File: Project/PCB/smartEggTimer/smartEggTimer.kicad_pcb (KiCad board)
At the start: 2 copper layers, 70 x 70 mm, 0 parts

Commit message: corrections and refinements for the schematic
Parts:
- added C1: 10u, Capacitor_SMD:C_0603_1608Metric, F.Cu at (192.1, 114.6)
- added C10: 4u7, Capacitor_SMD:C_0603_1608Metric, F.Cu at (192.1, 122.1)
- added C11: 4u7, Capacitor_SMD:C_0603_1608Metric, F.Cu at (192.1, 124.6)
- added C12: 10n, Capacitor_SMD:C_0805_2012Metric, F.Cu at (199.5, 141.0)
- added C13: 10n, Capacitor_SMD:C_0805_2012Metric, F.Cu at (199.5, 144.1)
- added C14: 100n, Capacitor_SMD:C_0402_1005Metric, F.Cu at (222.6, 124.8)
- added C15: 1u, Capacitor_SMD:C_0603_1608Metric, F.Cu at (192.1, 127.1)
- added C16: 1u, Capacitor_SMD:C_0603_1608Metric, F.Cu at (192.1, 129.6)
- added C17: 1u, Capacitor_SMD:C_0603_1608Metric, F.Cu at (198.6, 113.5)
- added C18: 1u, Capacitor_SMD:C_0603_1608Metric, F.Cu at (198.6, 116.0)
- added C2: 100n, Capacitor_SMD:C_0402_1005Metric, F.Cu at (222.6, 114.9)
- added C3: 100n, Capacitor_SMD:C_0402_1005Metric, F.Cu at (222.6, 116.9)
- added C4: 100n, Capacitor_SMD:C_0402_1005Metric, F.Cu at (222.6, 118.9)
- added C5: 100n, Capacitor_SMD:C_0402_1005Metric, F.Cu at (222.6, 120.8)
- added C6: 100n, Capacitor_SMD:C_0402_1005Metric, F.Cu at (222.6, 122.8)
- added C7: 10n, Capacitor_SMD:C_0805_2012Metric, F.Cu at (199.5, 138.0)
- added C8: 1u, Capacitor_SMD:C_0603_1608Metric, F.Cu at (192.1, 117.1)
- added C9: 1u, Capacitor_SMD:C_0603_1608Metric, F.Cu at (192.1, 119.6)
- added DFPlayerMini1: ~, custom-parts:DFplayer-Mini, F.Cu at (145.8, 70.5)
- added FB1: 120R, Inductor_SMD:L_0603_1608Metric, F.Cu at (155.7, 83.6)
- added H1: MountingHole, MountingHole:MountingHole_4.3mm_M4, F.Cu at (124.2, 72.3)
- added H2: MountingHole, MountingHole:MountingHole_4.3mm_M4, F.Cu at (120.5, 108.1)
- added H3: MountingHole, MountingHole:MountingHole_4.3mm_M4_DIN965, F.Cu at (172.0, 75.2)
- added H8: MountingHole, MountingHole:MountingHole_4.3mm_M4_DIN965, F.Cu at (172.9, 106.5)
- added J1: Conn_01x05_Pin, Connector_PinHeader_2.54mm:PinHeader_1x05_P2.54mm_Vertical, F.Cu at (132.0, 109.2)
- added J2: Conn_01x02_Pin, Connector_PinHeader_2.54mm:PinHeader_1x01_P2.54mm_Vertical, F.Cu at (168.3, 46.0)
- added J3: Conn_01x02_Pin, Connector_PinHeader_2.54mm:PinHeader_1x01_P2.54mm_Vertical, F.Cu at (168.3, 50.7)
- added J5: Conn_01x02_Socket, Connector_PinHeader_2.54mm:PinHeader_1x02_P2.54mm_Vertical, F.Cu at (115.8, 100.3)
- added J6: Conn_01x02_Socket, Connector_PinHeader_2.54mm:PinHeader_1x02_P2.54mm_Vertical, F.Cu at (117.0, 79.6)
- added J7: Conn_01x03_Pin, Connector_PinHeader_2.54mm:PinHeader_1x03_P2.54mm_Vertical, F.Cu at (150.1, 109.0)
- added OLED-15W-C1: ~, Connector_PinSocket_2.54mm:PinSocket_1x07_P2.54mm_Vertical, F.Cu at (130.8, 63.4)
- added Q1: STP60NF06L, Package_TO_SOT_THT:TO-220-3_Vertical, F.Cu at (127.5, 88.7)
- added R1: 4k7, Resistor_SMD:R_0402_1005Metric, F.Cu at (202.0, 115.6)
- added R10: 10k, Resistor_SMD:R_0402_1005Metric, F.Cu at (209.5, 124.9)
- added R11: 10k, Resistor_SMD:R_0402_1005Metric, F.Cu at (209.5, 126.9)
- added R12: 1M, Resistor_SMD:R_0402_1005Metric, F.Cu at (209.5, 128.9)
- added R13: 1M, Resistor_SMD:R_0402_1005Metric, F.Cu at (209.5, 130.9)
- added R14: 10k, Resistor_SMD:R_0402_1005Metric, F.Cu at (209.5, 132.9)
- added R15: 22k, Resistor_SMD:R_0402_1005Metric, F.Cu at (216.4, 114.9)
- added R16: 10k, Resistor_SMD:R_0402_1005Metric, F.Cu at (216.4, 116.9)
- added R17: 22k, Resistor_SMD:R_0402_1005Metric, F.Cu at (216.4, 118.8)
- added R18: 10k, Resistor_SMD:R_0402_1005Metric, F.Cu at (216.4, 120.8)
- added R19: 22k, Resistor_SMD:R_0402_1005Metric, F.Cu at (216.4, 122.8)
- added R2: 10k, Resistor_SMD:R_0402_1005Metric, F.Cu at (202.0, 117.5)
- added R20: 10k, Resistor_SMD:R_0402_1005Metric, F.Cu at (216.4, 124.8)
- added R21: 22k, Resistor_SMD:R_0402_1005Metric, F.Cu at (216.4, 126.8)
- added R3: 1k, Resistor_SMD:R_0402_1005Metric, F.Cu at (202.0, 119.5)
- added R4: 100k, Resistor_SMD:R_0402_1005Metric, F.Cu at (202.0, 121.5)
- added R5: 100, Resistor_SMD:R_0402_1005Metric, F.Cu at (202.0, 123.5)
- added R6: 4k7, Resistor_SMD:R_0402_1005Metric, F.Cu at (202.0, 125.5)
- added R7: 4k7, Resistor_SMD:R_0402_1005Metric, F.Cu at (202.0, 127.5)
- added R8: 10k, Resistor_SMD:R_0402_1005Metric, F.Cu at (209.6, 115.3)
- added R9: 10k, Resistor_SMD:R_0402_1005Metric, F.Cu at (209.6, 120.7)
- added SW1: SW_Push_Dual, Button_Switch_THT:SW_PUSH_6mm_H9.5mm, F.Cu at (159.6, 64.8)
- added SW2: EC12E24204A2, Rotary_Encoder:RotaryEncoder_Alps_EC12E_Vertical_H20mm, F.Cu at (167.8, 90.9)
- added SW3: SW_Push_Dual, Button_Switch_THT:SW_PUSH_6mm_H13mm, F.Cu at (113.2, 88.8)
- added SW4: SW_Push_Dual, Button_Switch_THT:SW_PUSH_6mm_H13mm, F.Cu at (130.1, 115.2)
- added SW5: SW_Push_Dual, Button_Switch_THT:SW_PUSH_6mm_H13mm, F.Cu at (144.2, 115.2)
- added SW6: SW_Push_Dual, Button_Switch_THT:SW_PUSH_6mm_H13mm, F.Cu at (157.1, 115.4)
- added SW7: SW_SPDT, Button_Switch_THT:SW_Slide_SPDT_Angled_CK_OS102011MA1Q, F.Cu at (146.2, 127.0)
- added U1: STM32F103RET6, Package_QFP:LQFP-64_10x10mm_P0.5mm, F.Cu at (148.1, 91.2)
- added U3: AP7361C-33E, Package_TO_SOT_SMD:SOT-223-3_TabPin2, F.Cu at (151.5, 69.1)
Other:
- board size 70 x 70 mm -> 72 x 72 mm
- board text added: "diameter of the PCB has to be 72mm with 4 holes, each 21.5mm in both direction from the center away The center of the rotary encoder has to be 30mm from the center away the 4 buttons also have a fixed position as soon as we finished the CAD model"
- board text removed: "diameter of the PCB has to be 70mm with 4 holes, each 21.5mm in both direction from the center away The center of the rotary encoder has to be 30mm from the center away the 4 buttons also have a fixed position as soon as we finished the CAD model"

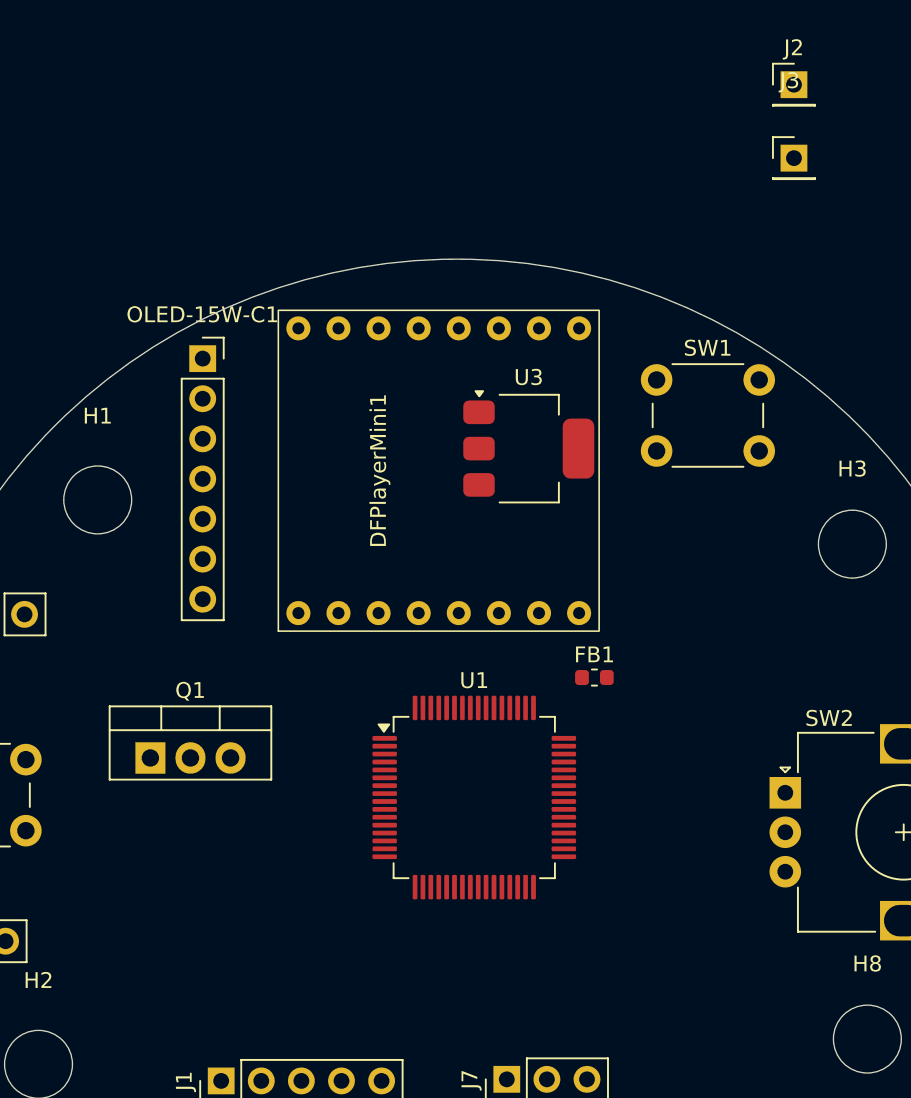
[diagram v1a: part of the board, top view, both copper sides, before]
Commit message: add pin numbers for display
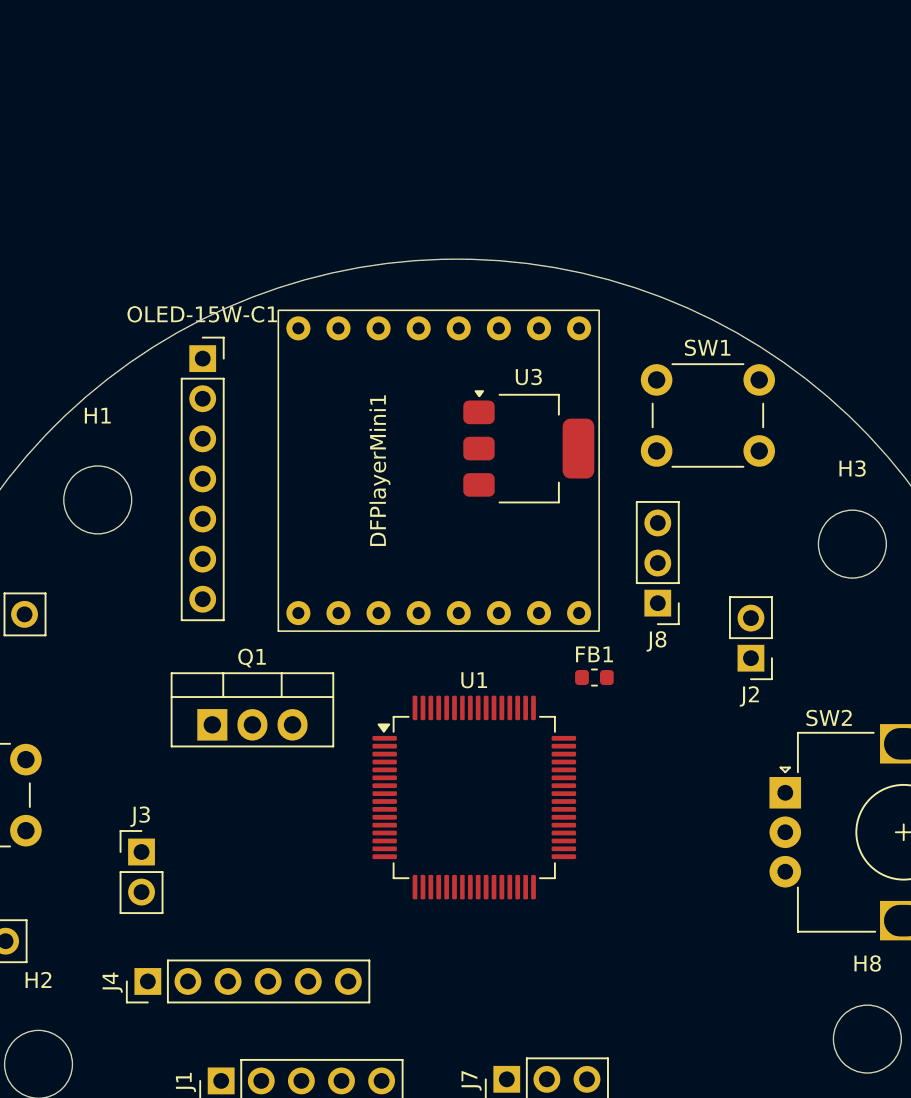
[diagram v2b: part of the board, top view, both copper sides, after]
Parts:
- added J4: Conn_01x06_Pin, Connector_PinHeader_2.54mm:PinHeader_1x06_P2.54mm_Vertical, F.Cu at (127.4, 102.8)
- added J8: Conn_01x03_Pin, Connector_PinHeader_2.54mm:PinHeader_1x03_P2.54mm_Vertical, F.Cu at (159.7, 78.9)
- J2, J3: footprint Connector_PinHeader_2.54mm:PinHeader_1x01_P2.54mm_Vertical -> Connector_PinHeader_2.54mm:PinHeader_1x02_P2.54mm_Vertical
- moved J3 60.3 mm to (127.0, 94.7)
- moved J2 36.4 mm to (165.6, 82.4), turned to 180 degrees
- moved Q1 4.45 mm to (131.5, 86.6)
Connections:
- OLED-15W-C1 pad 1: (no net) -> +3.3V
- OLED-15W-C1 pad 2: (no net) -> GND
- OLED-15W-C1 pad 3: (no net) -> /I2C1_SDA
- OLED-15W-C1 pad 4: (no net) -> /I2C_SCL
- OLED-15W-C1 pad 5: (no net) -> unconnected-(OLED-15W-C1-CS-Pad5)
- OLED-15W-C1 pad 6: (no net) -> unconnected-(OLED-15W-C1-D/C-Pad6)
- OLED-15W-C1 pad 7: (no net) -> /display_reset

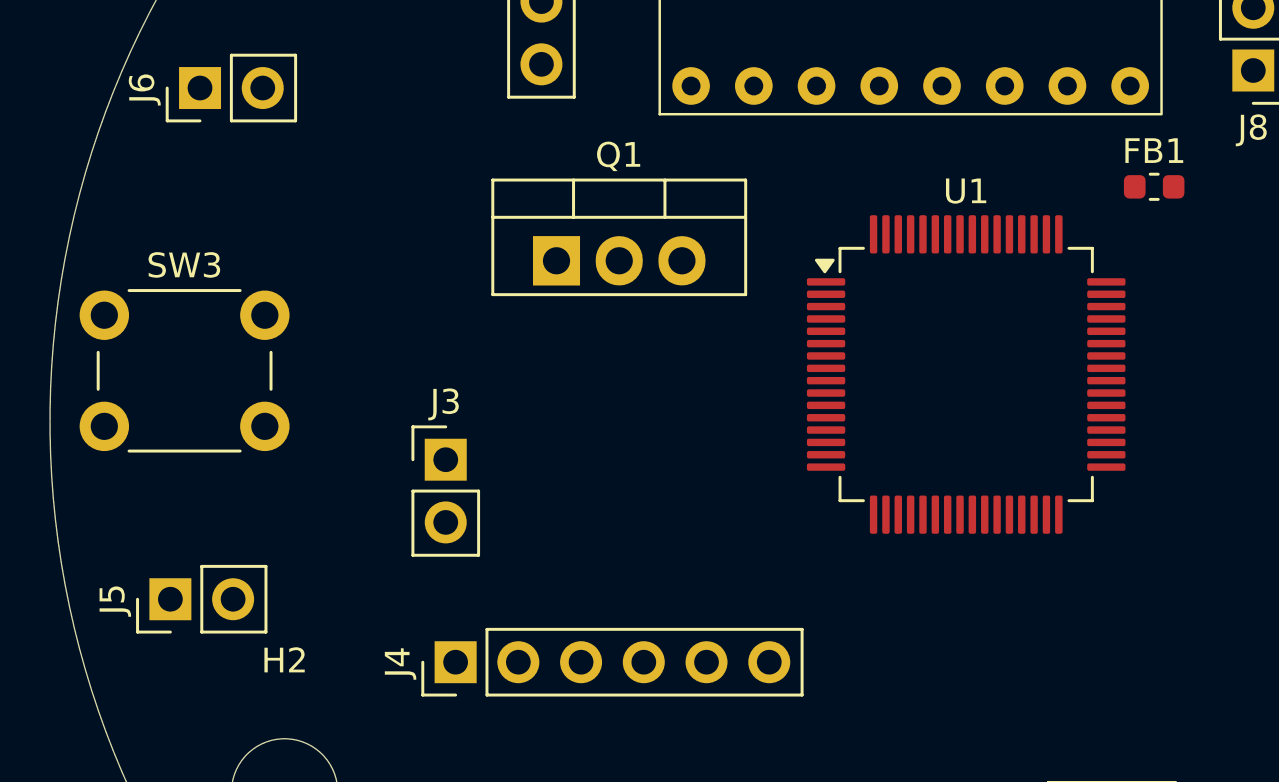
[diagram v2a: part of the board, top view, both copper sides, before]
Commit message: add pin numbers for DFplayer and re-add DFplayer footprint
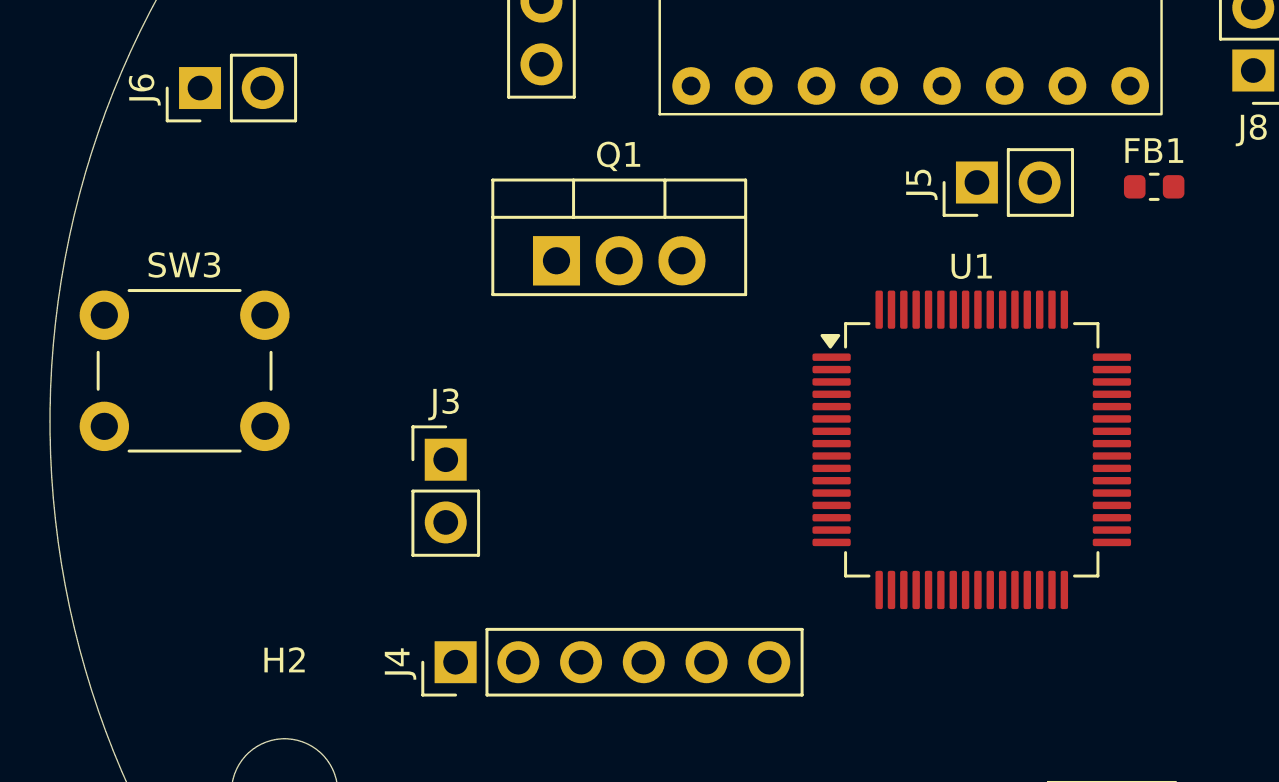
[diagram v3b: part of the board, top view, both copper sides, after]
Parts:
- moved J5 36.8 mm to (148.5, 83.4)
- moved U1 3.06 mm to (148.3, 94.2)
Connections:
- DFPlayerMini1 pad 1: (no net) -> /Battery-SW
- DFPlayerMini1 pad 10: (no net) -> Net-(Q1-D)
- DFPlayerMini1 pad 11: (no net) -> unconnected-(DFPlayerMini1-IO_2-Pad11)
- DFPlayerMini1 pad 12: (no net) -> unconnected-(DFPlayerMini1-ADKEY_1-Pad12)
- DFPlayerMini1 pad 13: (no net) -> unconnected-(DFPlayerMini1-ADKEY_2-Pad13)
- DFPlayerMini1 pad 14: (no net) -> unconnected-(DFPlayerMini1-USB+-Pad14)
- DFPlayerMini1 pad 15: (no net) -> unconnected-(DFPlayerMini1-USB--Pad15)
- DFPlayerMini1 pad 16: (no net) -> unconnected-(DFPlayerMini1-BUSY-Pad16)
- DFPlayerMini1 pad 2: (no net) -> Net-(DFPlayerMini1-RX)
- DFPlayerMini1 pad 3: (no net) -> /UART2_TX
- DFPlayerMini1 pad 4: (no net) -> /DAC_R
- DFPlayerMini1 pad 5: (no net) -> /DAC_L
- DFPlayerMini1 pad 6: (no net) -> /SPK+
- DFPlayerMini1 pad 7: (no net) -> Net-(Q1-D)
- DFPlayerMini1 pad 8: (no net) -> /SPK-
- DFPlayerMini1 pad 9: (no net) -> unconnected-(DFPlayerMini1-IO_1-Pad9)
- Q1 pad 1: Net-(DFPlayerMini1-GND) -> Net-(Q1-D)
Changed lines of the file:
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@@
 	(net 7 "Net-(Q1-G)")
 	(net 8 "/Rotary Encoder b")
-	(net 9 "Net-(DFPlayerMini1-GND)")
+	(net 9 "Net-(Q1-D)")
 	(net 10 "/Battery_indicator")
 	(net 11 "/Button_1")
@@
 	(net 80 "unconnected-(OLED-15W-C1-D{slash}C-Pad6)")
 	(net 81 "unconnected-(OLED-15W-C1-CS-Pad5)")
+	(net 82 "unconnected-(DFPlayerMini1-ADKEY_1-Pad12)")
+	(net 83 "unconnected-(DFPlayerMini1-USB--Pad15)")
+	(net 84 "unconnected-(DFPlayerMini1-IO_2-Pad11)")
+	(net 85 "unconnected-(DFPlayerMini1-IO_1-Pad9)")
+	(net 86 "unconnected-(DFPlayerMini1-BUSY-Pad16)")
+	(net 87 "unconnected-(DFPlayerMini1-USB+-Pad14)")
+	(net 88 "unconnected-(DFPlayerMini1-ADKEY_2-Pad13)")
 	(footprint "Button_Switch_THT:SW_PUSH_6mm_H13mm"
 		(layer "F.Cu")
@@
 			(layers "*.Cu" "*.Mask")
 			(remove_unused_layers no)
+			(net 4 "/Battery-SW")
+			(pinfunction "VCC")
+			(pintype "input")
 		)
 		(pad "2" thru_hole circle
@@
 			(layers "*.Cu" "*.Mask")
 			(remove_unused_layers no)
+			(net 27 "Net-(DFPlayerMini1-RX)")
+			(pinfunction "RX")
+			(pintype "input")
 		)
 		(pad "3" thru_hole circle
@@
 			(layers "*.Cu" "*.Mask")
 			(remove_unused_layers no)
+			(net 59 "/UART2_TX")
+			(pinfunction "TX")
+			(pintype "input")
 		)
 		(pad "4" thru_hole circle
@@
 			(layers "*.Cu" "*.Mask")
 			(remove_unused_layers no)
+			(net 79 "/DAC_R")
+			(pinfunction "DAC_R")
+			(pintype "input")
 		)
 		(pad "5" thru_hole circle
@@
 			(layers "*.Cu" "*.Mask")
 			(remove_unused_layers no)
+			(net 78 "/DAC_L")
+			(pinfunction "DAC_L")
+			(pintype "input")
 		)
 		(pad "6" thru_hole circle
@@
 			(layers "*.Cu" "*.Mask")
 			(remove_unused_layers no)
+			(net 20 "/SPK+")
+			(pinfunction "SPK_1")
+			(pintype "input")
 		)
 		(pad "7" thru_hole circle
@@
 			(layers "*.Cu" "*.Mask")
 			(remove_unused_layers no)
+			(net 9 "Net-(Q1-D)")
+			(pinfunction "GND")
+			(pintype "input")
 		)
 		(pad "8" thru_hole circle
@@
 			(layers "*.Cu" "*.Mask")
 			(remove_unused_layers no)
+			(net 21 "/SPK-")
+			(pinfunction "SPK_2")
+			(pintype "input")
 		)
 		(pad "9" thru_hole circle
-			(at 9.017 -8.89 90)
+			(at 9.017 8.89 90)
 			(size 1.524 1.524)
 			(drill 0.762)
 			(layers "*.Cu" "*.Mask")
 			(remove_unused_layers no)
+			(net 85 "unconnected-(DFPlayerMini1-IO_1-Pad9)")
+			(pinfunction "IO_1")
+			(pintype "input+no_connect")
 		)
 		(pad "10" thru_hole circle
-			(at 9.017 -6.35 90)
+			(at 9.017 6.35 90)
 			(size 1.524 1.524)
 			(drill 0.762)
 			(layers "*.Cu" "*.Mask")
 			(remove_unused_layers no)
+			(net 9 "Net-(Q1-D)")
+			(pinfunction "GND")
+			(pintype "input")
 		)
 		(pad "11" thru_hole circle
-			(at 9.017 -3.81 90)
+			(at 9.017 3.81 90)
 			(size 1.524 1.524)
 			(drill 0.762)
 			(layers "*.Cu" "*.Mask")
 			(remove_unused_layers no)
+			(net 84 "unconnected-(DFPlayerMini1-IO_2-Pad11)")
+			(pinfunction "IO_2")
+			(pintype "input+no_connect")
 		)
 		(pad "12" thru_hole circle
-			(at 9.017 -1.27 90)
+			(at 9.017 1.27 90)
 			(size 1.524 1.524)
 			(drill 0.762)
 			(layers "*.Cu" "*.Mask")
 			(remove_unused_layers no)
+			(net 82 "unconnected-(DFPlayerMini1-ADKEY_1-Pad12)")
+			(pinfunction "ADKEY_1")
+			(pintype "input+no_connect")
 		)
 		(pad "13" thru_hole circle
-			(at 9.017 1.27 90)
+			(at 9.017 -1.27 90)
 			(size 1.524 1.524)
 			(drill 0.762)
 			(layers "*.Cu" "*.Mask")
 			(remove_unused_layers no)
+			(net 88 "unconnected-(DFPlayerMini1-ADKEY_2-Pad13)")
+			(pinfunction "ADKEY_2")
+			(pintype "input+no_connect")
 		)
 		(pad "14" thru_hole circle
-			(at 9.017 3.81 90)
+			(at 9.017 -3.81 90)
 			(size 1.524 1.524)
 			(drill 0.762)
 			(layers "*.Cu" "*.Mask")
 			(remove_unused_layers no)
+			(net 87 "unconnected-(DFPlayerMini1-USB+-Pad14)")
+			(pinfunction "USB+")
+			(pintype "input+no_connect")
 		)
 		(pad "15" thru_hole circle
-			(at 9.017 6.35 90)
+			(at 9.017 -6.35 90)
 			(size 1.524 1.524)
 			(drill 0.762)
 			(layers "*.Cu" "*.Mask")
 			(remove_unused_layers no)
+			(net 83 "unconnected-(DFPlayerMini1-USB--Pad15)")
+			(pinfunction "USB-")
+			(pintype "input+no_connect")
 		)
 		(pad "16" thru_hole circle
-			(at 9.017 8.89 90)
+			(at 9.017 -8.89 90)
 			(size 1.524 1.524)
 			(drill 0.762)
 			(layers "*.Cu" "*.Mask")
 			(remove_unused_layers no)
+			(net 86 "unconnected-(DFPlayerMini1-BUSY-Pad16)")
+			(pinfunction "BUSY")
+			(pintype "input+no_connect")
 		)
 	)
@@
 			(layers "*.Cu" "*.Mask")
 			(remove_unused_layers no)
-			(net 9 "Net-(DFPlayerMini1-GND)")
+			(net 9 "Net-(Q1-D)")
 			(pinfunction "D")
 			(pintype "passive")
@@
 	(footprint "Package_QFP:LQFP-64_10x10mm_P0.5mm"
 		(layer "F.Cu")
-		(at 148.05 91.2)
+		(at 148.275 94.25)
 		(descr "LQFP, 64 Pin (https://www.analog.com/media/en/technical-documentation/data-sheets/ad7606_7606-6_7606-4.pdf), generated with kicad-footprint-generator ipc_gullwing_generator.py")
 		(tags "LQFP QFP")
@@
 	(footprint "Connector_PinHeader_2.54mm:PinHeader_1x02_P2.54mm_Vertical"
 		(layer "F.Cu")
-		(at 115.825 100.3 90)
+		(at 148.485 83.425 90)
 		(descr "Through hole straight pin header, 1x02, 2.54mm pitch, single row")
 		(tags "Through hole pin header THT 1x02 2.54mm single row")
